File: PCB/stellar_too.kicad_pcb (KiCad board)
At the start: 2 copper layers, 139 x 121 mm, 60 parts, among them J1 USB_C_Receptacle_USB2.0_14P, J2 USB_C_Receptacle_USB2.0_16P, SW1 SW_Push_45deg, SW10 SW_Push_45deg, SW11 SW_Push_45deg, SW12 SW_Push_45deg, SW13 SW_Push_45deg, SW14 SW_Push_45deg, SW15 SW_Push_45deg, SW16 SW_Push_45deg, SW17 SW_Push_45deg, SW18 SW_Push_45deg, SW19 SW_Push_45deg, SW2 SW_Push_45deg, SW20 SW_Push_45deg, SW21 SW_Push_45deg, SW22 SW_Push_45deg, SW23 SW_Push_45deg, SW24 SW_Push_45deg, SW25 SW_Push_45deg, SW26 SW_Push_45deg, SW27 SW_Push_45deg, SW28 SW_Push_45deg, SW3 SW_Push_45deg, SW4 SW_Push_45deg, SW5 SW_Push_45deg, SW6 SW_Push_45deg, SW7 SW_Push_45deg, SW8 SW_Push_45deg, SW9 SW_Push_45deg, U1 MDBT50Q, U2 FUSB302B01MPX

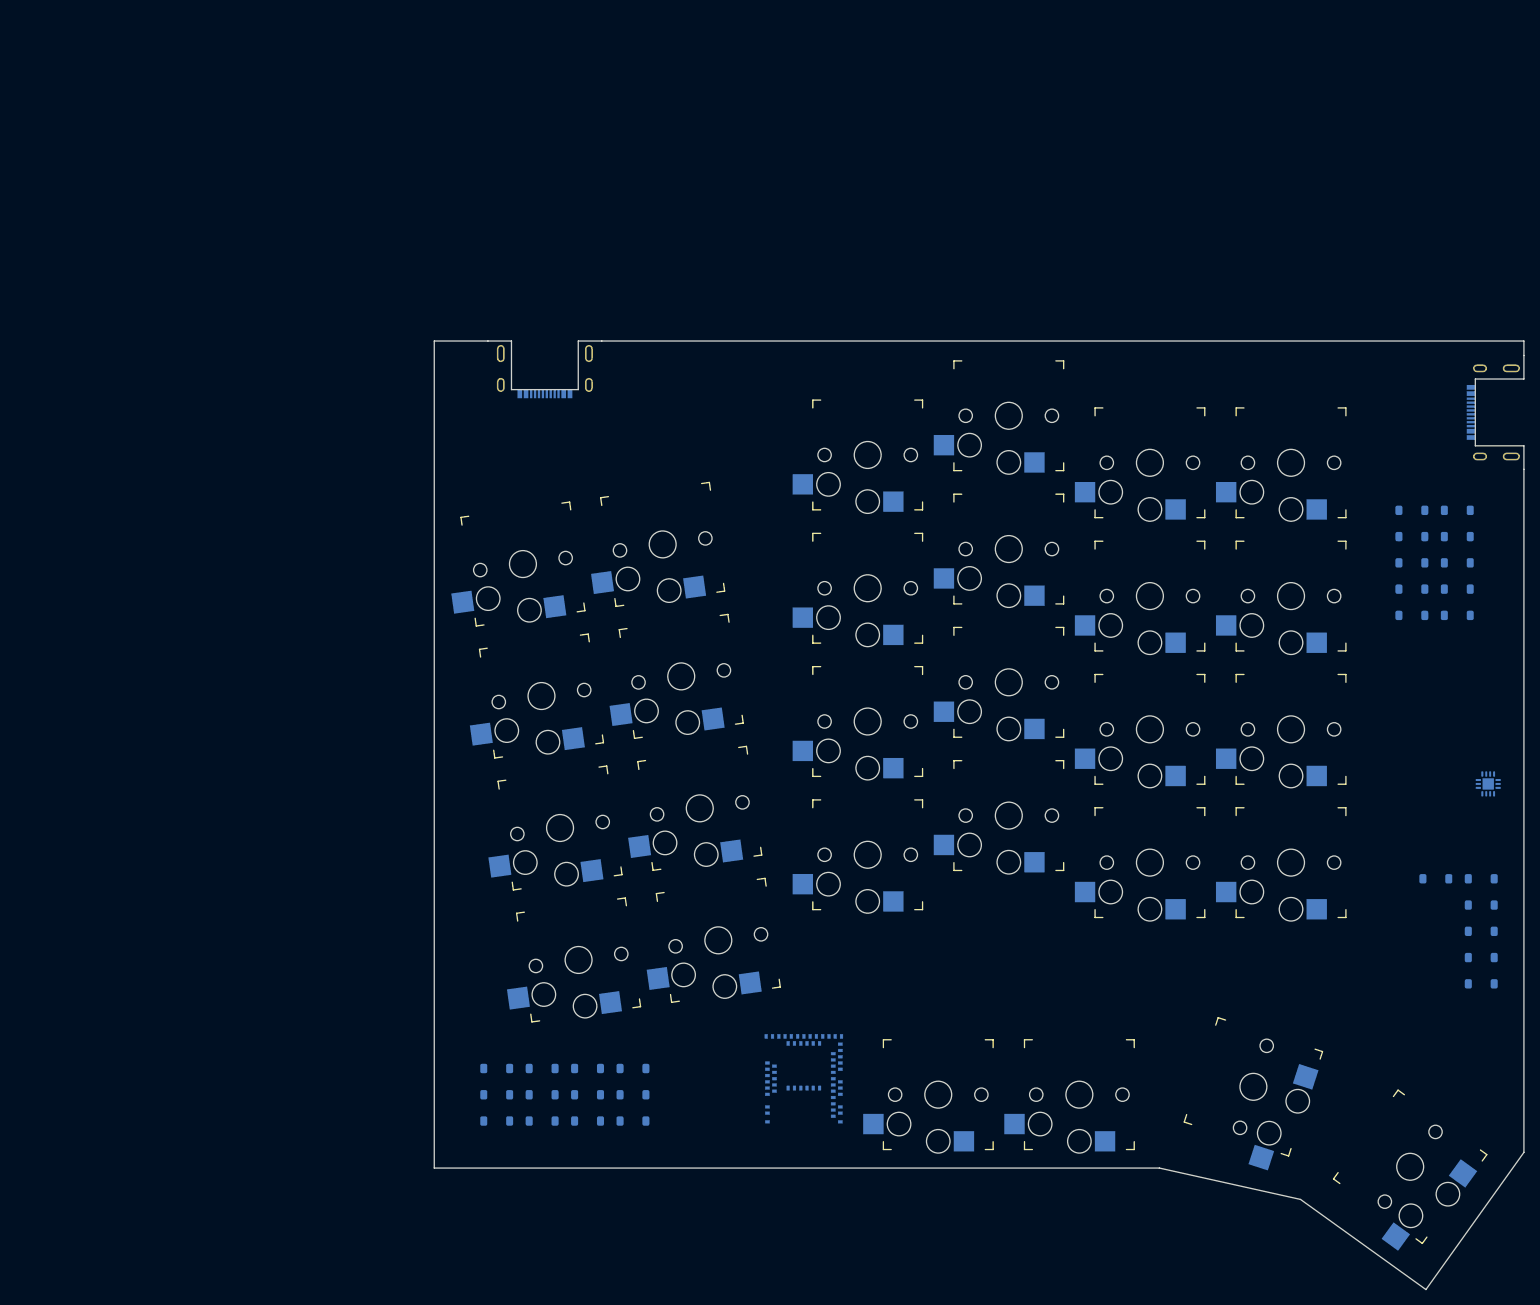
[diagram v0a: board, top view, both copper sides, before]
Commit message: feat(pcb) layout of keys changed
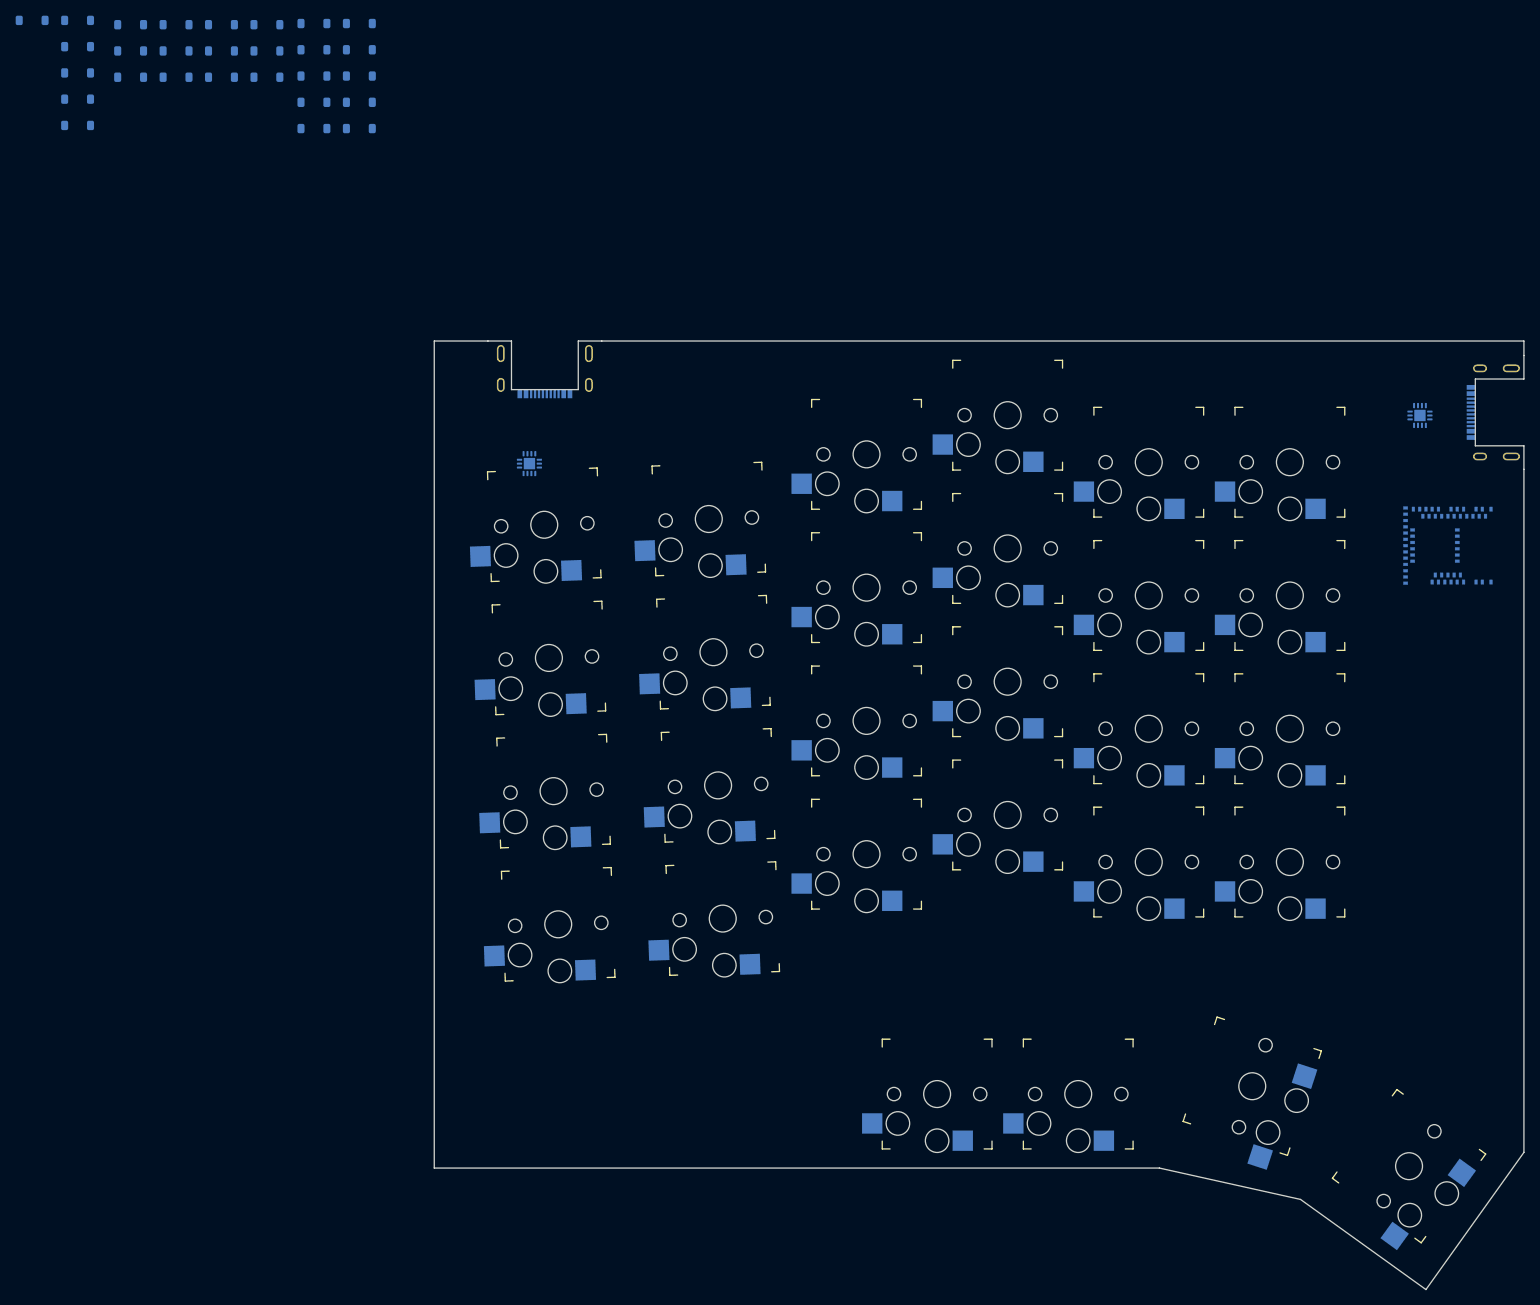
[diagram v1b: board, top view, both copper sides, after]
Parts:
- added U3: FUSB302B01MPX, Package_DFN_QFN:WQFN-14-1EP_2.5x2.5mm_P0.5mm_EP1.45x1.45mm, B.Cu at (88.6, 48.6)
- moved D20 209.9 mm to (31.0, -7.90)
- moved D21 209.9 mm to (31.0, -4.55)
- moved D22 209.9 mm to (31.0, -1.20)
- moved D23 209.9 mm to (31.0, 2.15)
- moved D24 209.9 mm to (31.0, 5.50)
- moved D28 209.9 mm to (25.2, -7.90)
- moved D12 153.2 mm to (61.1, -7.50)
- moved D13 153.2 mm to (61.1, -4.15)
- moved D14 153.2 mm to (61.1, -0.80)
- moved D15 153.2 mm to (61.1, 2.55)
- moved D16 153.2 mm to (61.1, 5.90)
- moved D4 153.2 mm to (66.9, -7.50)
- moved D5 153.2 mm to (66.9, -4.15)
- moved D6 153.2 mm to (66.9, -0.80)
- moved D7 153.2 mm to (66.9, 2.55)
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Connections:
- J1 pad A1: Net-(J1-GND-PadA1) -> GND
- J1 pad A12: Net-(J1-GND-PadA1) -> GND
- J2 pad A5: unconnected-(J2-CC1-PadA5) -> Net-(J2-CC1)
- J2 pad B5: unconnected-(J2-CC2-PadB5) -> Net-(J2-CC2)
- U1 pad 1: Net-(U1-GND-Pad1) -> GND
- U1 pad 15: Net-(U1-GND-Pad1) -> GND
- U1 pad 2: Net-(U1-GND-Pad1) -> GND
- U1 pad 33: Net-(U1-GND-Pad1) -> GND
- U1 pad 34: unconnected-(U1-D--Pad34) -> /D-
- U1 pad 35: unconnected-(U1-D+-Pad35) -> /D+
- U1 pad 40: unconnected-(U1-P1.18/RESET-Pad40) -> Net-(U1-P1.18/RESET)
- U1 pad 55: Net-(U1-GND-Pad1) -> GND
- U2 pad 1: Net-(U2-CC2-Pad1) -> Net-(J2-CC2)
- U2 pad 10: Net-(U2-CC1-Pad10) -> Net-(J2-CC1)
- U2 pad 11: Net-(U2-CC1-Pad10) -> Net-(J2-CC1)
- U2 pad 14: Net-(U2-CC2-Pad1) -> Net-(J2-CC2)
